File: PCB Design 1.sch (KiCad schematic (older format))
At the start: 38 parts, among them Q1 MMBT3906, Q2 MMBT3906, Q3 MMBT3906, Q4 MMBT3906, Q5 MMBT3906, Q6 MMBT3906, Q7 MMBT3906, Q8 MMBT3906, SW1 SW_PUSH, SW2 SW_PUSH, U1 MAX6969, U2 MAX6969, U3 74HC595, U4 CD4051B, U7 74125/126

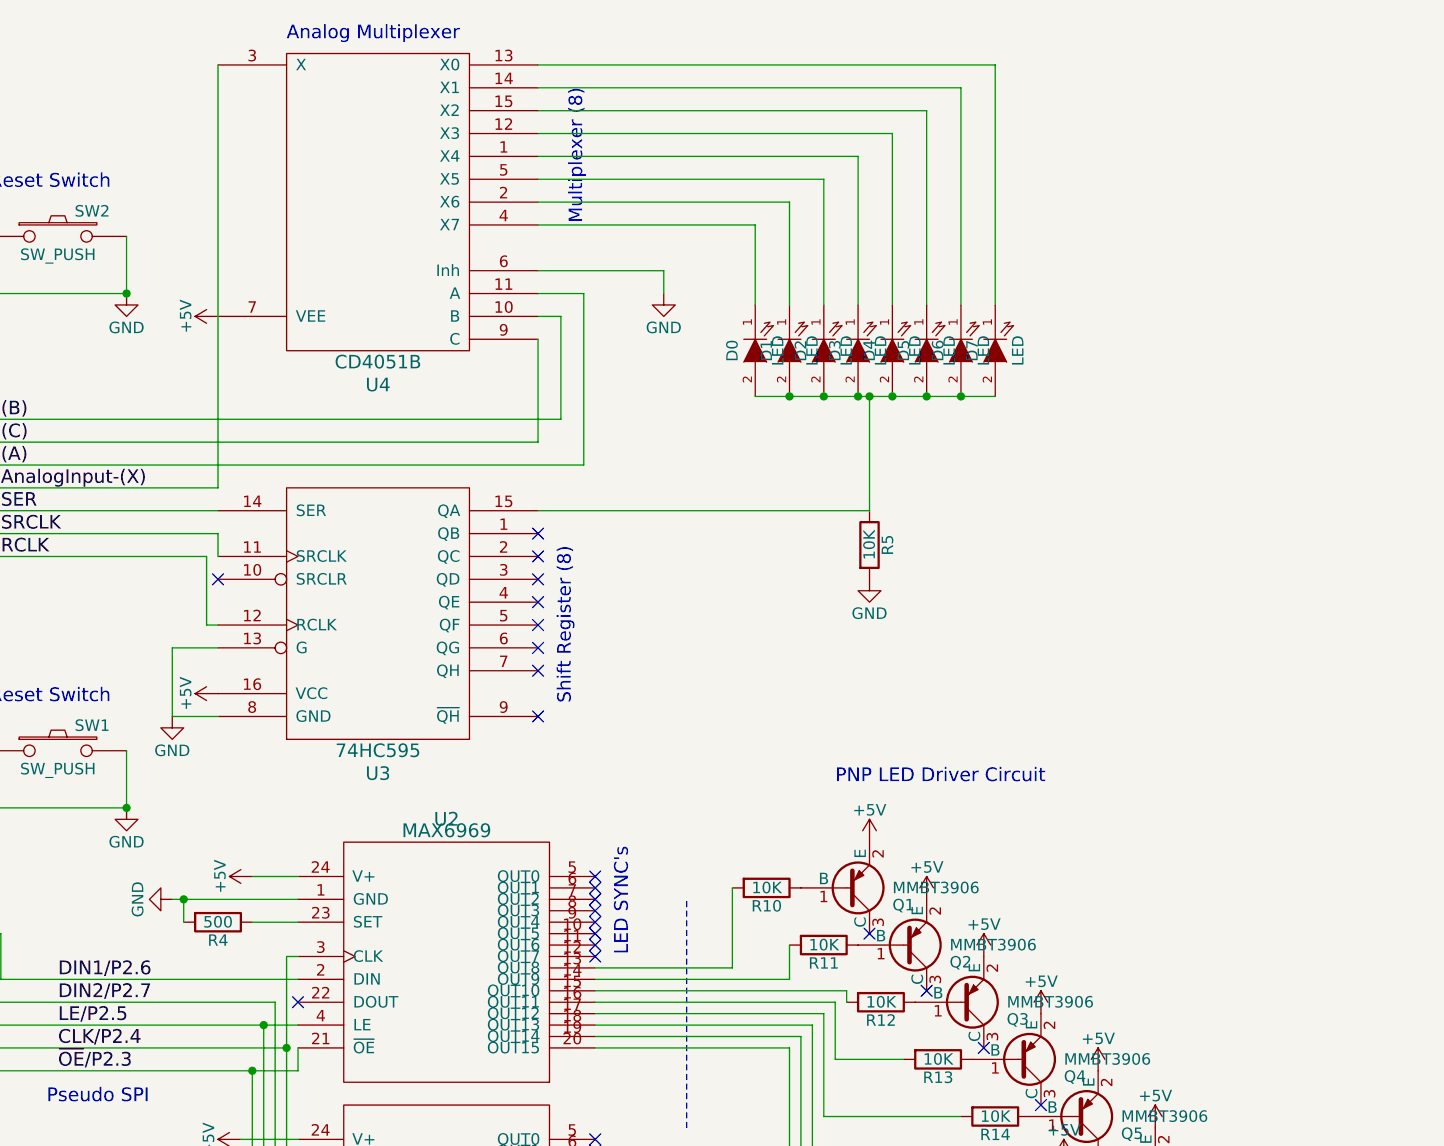
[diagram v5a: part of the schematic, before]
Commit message: IR LED fix
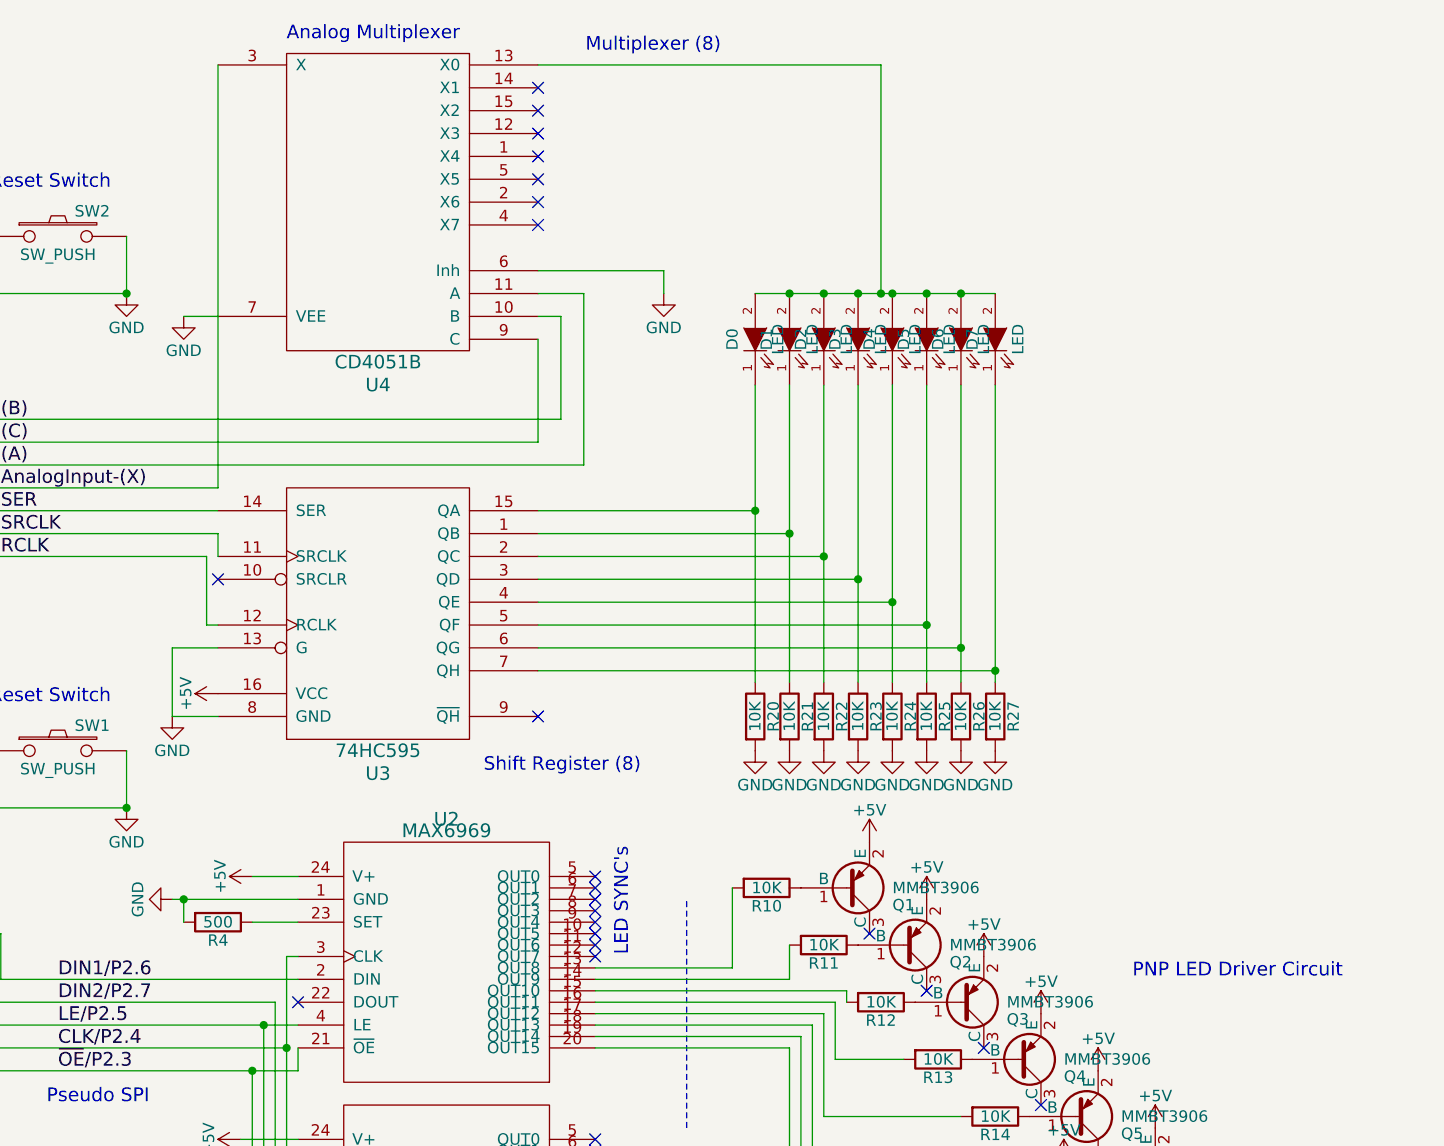
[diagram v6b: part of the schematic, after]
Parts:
- added R21, R22, R23, R24, R25, R26, R27: 10K, symbol R
- renumbered R5 to R20
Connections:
- net +5V: no longer U4.7 (VEE)
- net GND: now also U4.7 (VEE), R21.2, R22.2, R23.2, R24.2, R25.2, R26.2, R27.2
- net at U3.1 (QB): now also D1.1 (K), R21.1
- net at D0.2 (A), D1.2 (A), D2.2 (A)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: now also U4.13 (X0); no longer R20.1, U3.15 (QA)
- net at U3.2 (QC): now also D2.1 (K), R22.1
- net at U3.3 (QD): now also D3.1 (K), R23.1
- net at U3.4 (QE): now also D4.1 (K), R24.1
- net at U3.5 (QF): now also D5.1 (K), R25.1
- net at U3.6 (QG): now also D6.1 (K), R26.1
- net at U3.7 (QH): now also D7.1 (K), R27.1
- net at U4.1 (X4): no longer D3.1 (K)
- net at U4.12 (X3): no longer D4.1 (K)
- net at U4.14 (X1): no longer D6.1 (K)
- net at U4.15 (X2): no longer D5.1 (K)
- net at U4.2 (X6): no longer D1.1 (K)
- net at D0.1 (K): now also R20.1, U3.15 (QA); no longer U4.4 (X7)
- net at U4.5 (X5): no longer D2.1 (K)
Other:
- moved on the sheet: D0, D1, D2, D3, D4, D5, D6, D7, R20
